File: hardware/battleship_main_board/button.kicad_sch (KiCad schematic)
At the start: 2 parts

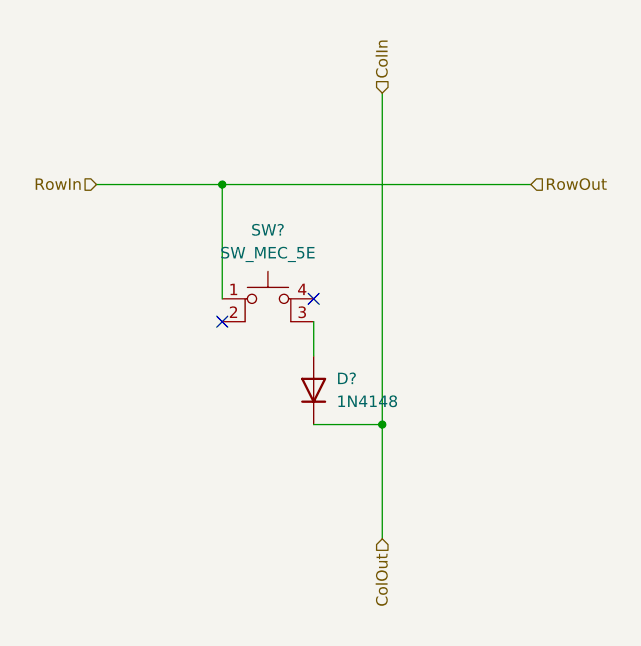
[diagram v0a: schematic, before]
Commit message: Got schematic to place that can be turned into a ratsnest
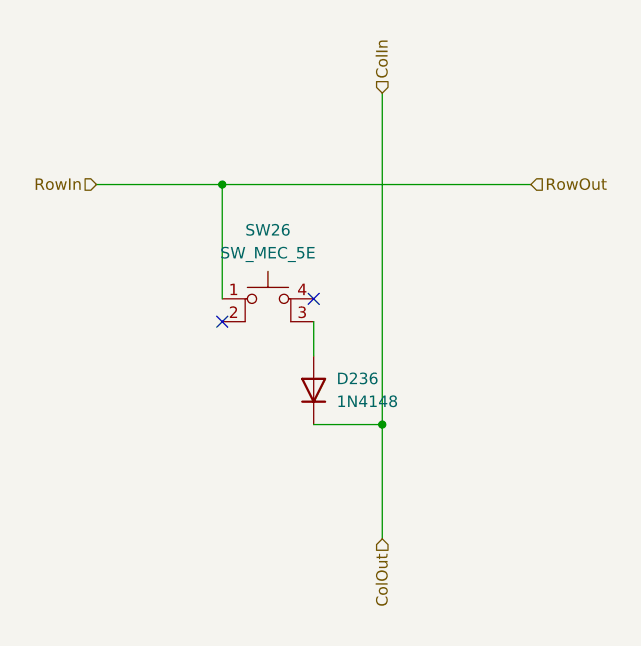
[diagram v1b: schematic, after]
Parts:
- SW26: renamed from SW?; footprint (none) -> Button_Switch_THT:SW_PUSH_6mm
- gave numbers to parts that had none: 1
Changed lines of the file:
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@@
   (symbol (lib_id "Diode:1N4148") (at 139.7 81.28 90)
     (in_bom yes) (on_board yes) (fields_autoplaced)
-    (property "Reference" "D?" (id 0) (at 142.24 80.0099 90)
+    (property "Reference" "D236" (id 0) (at 142.24 80.0099 90)
       (effects (font (size 1.27 1.27)) (justify right))
     )
@@
   (symbol (lib_id "Switch:SW_MEC_5E") (at 134.62 73.66 0)
     (in_bom yes) (on_board yes) (fields_autoplaced)
-    (property "Reference" "SW?" (id 0) (at 134.62 63.5 0))
+    (property "Reference" "SW26" (id 0) (at 134.62 63.5 0))
     (property "Value" "SW_MEC_5E" (id 1) (at 134.62 66.04 0))
-    (property "Footprint" "" (id 2) (at 134.62 66.04 0)
+    (property "Footprint" "Button_Switch_THT:SW_PUSH_6mm" (id 2) (at 134.62 66.04 0)
       (effects (font (size 1.27 1.27)) hide)
     )

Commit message: Fixed annotations so that button rows are in order
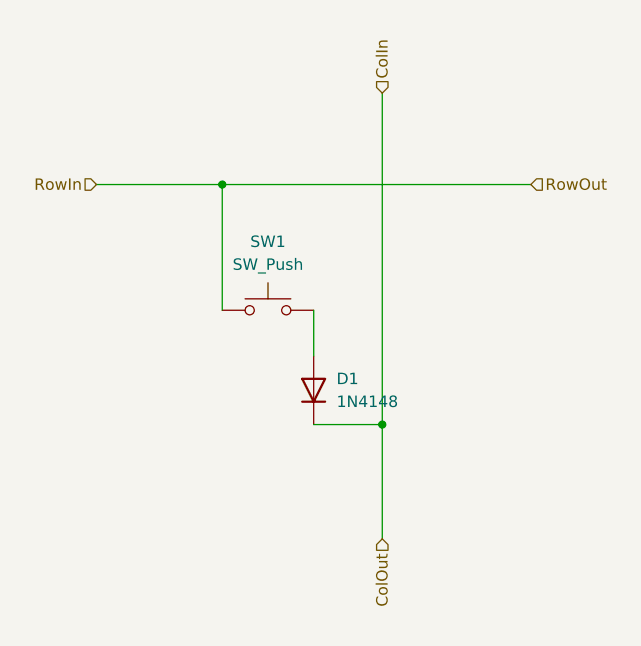
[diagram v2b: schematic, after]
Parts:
- removed SW26: SW_MEC_5E, Button_Switch_THT:SW_PUSH_6mm, symbol Switch:SW_MEC_5E
- added SW1: SW_Push, Button_Switch_THT:SW_PUSH_6mm, symbol Switch:SW_Push
- renumbered D236 to D1
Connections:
- net RowIn: now also SW1.1
- net at D1.2 (A): now also SW1.2
- no-connect marks 2 -> 0
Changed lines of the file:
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@@
   (junction (at 147.32 85.09) (diameter 0) (color 0 0 0 0)
   )
-  (no_connect (at 139.7 71.12))
-  (no_connect (at 129.54 73.66))
   (wire (pts (xy 115.57 58.42) (xy 129.54 58.42))
     (stroke (width 0) (type default) (color 0 0 0 0))
@@
     (stroke (width 0) (type default) (color 0 0 0 0))
   )
-  (wire (pts (xy 129.54 58.42) (xy 129.54 71.12))
+  (wire (pts (xy 129.54 58.42) (xy 129.54 72.39))
     (stroke (width 0) (type default) (color 0 0 0 0))
   )
@@
     (stroke (width 0) (type default) (color 0 0 0 0))
   )
-  (wire (pts (xy 139.7 73.66) (xy 139.7 77.47))
+  (wire (pts (xy 139.7 72.39) (xy 139.7 77.47))
     (stroke (width 0) (type default) (color 0 0 0 0))
   )
@@
   (symbol (lib_id "Diode:1N4148") (at 139.7 81.28 90)
     (in_bom yes) (on_board yes) (fields_autoplaced)
-    (property "Reference" "D236" (id 0) (at 142.24 80.0099 90)
+    (property "Reference" "D1" (id 0) (at 142.24 80.0099 90)
       (effects (font (size 1.27 1.27)) (justify right))
     )
@@
     (pin "2")
   )
-  (symbol (lib_id "Switch:SW_MEC_5E") (at 134.62 73.66 0)
+  (symbol (lib_id "Switch:SW_Push") (at 134.62 72.39 0)
     (in_bom yes) (on_board yes) (fields_autoplaced)
-    (property "Reference" "SW26" (id 0) (at 134.62 63.5 0))
-    (property "Value" "SW_MEC_5E" (id 1) (at 134.62 66.04 0))
-    (property "Footprint" "Button_Switch_THT:SW_PUSH_6mm" (id 2) (at 134.62 66.04 0)
+    (property "Reference" "SW1" (id 0) (at 134.62 64.77 0))
+    (property "Value" "SW_Push" (id 1) (at 134.62 67.31 0))
+    (property "Footprint" "Button_Switch_THT:SW_PUSH_6mm" (id 2) (at 134.62 67.31 0)
       (effects (font (size 1.27 1.27)) hide)
     )
-    (property "Datasheet" "http://www.apem.com/int/index.php?controller=attachment&id_attachment=1371" (id 3) (at 134.62 66.04 0)
+    (property "Datasheet" "~" (id 3) (at 134.62 67.31 0)
       (effects (font (size 1.27 1.27)) hide)
     )
     (pin "1")
     (pin "2")
-    (pin "3")
-    (pin "4")
   )
 )
